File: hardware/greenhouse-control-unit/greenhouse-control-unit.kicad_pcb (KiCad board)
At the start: 4 copper layers, 150 x 90 mm, 53 parts, among them J1 Buck_Conn_01x01_Female, J10 Conn_ESP32_DevKitV1_Female, J12 Conn_01x05_Female, J13 Beep_Jumper, J15 Conn_01x05_Female, J16 Conn_01x05_Female, J2 Buck_Conn_01x01_Female, J3 Buck_Conn_01x01_Female, J4 Buck_Conn_01x01_Female, J5 Molex_KK-396_01x02, J6 Molex_KK-396_01x02, J7 Molex_KK-396_01x12, J8 Molex_KK-254_01x12, J9 Conn_01x09, Q1 BC547, Q2 BC547, Q3 BC547, Q4 BC547, Q5 2N3906, Q7 BC337, Q8 BC337, U1 PCF8574

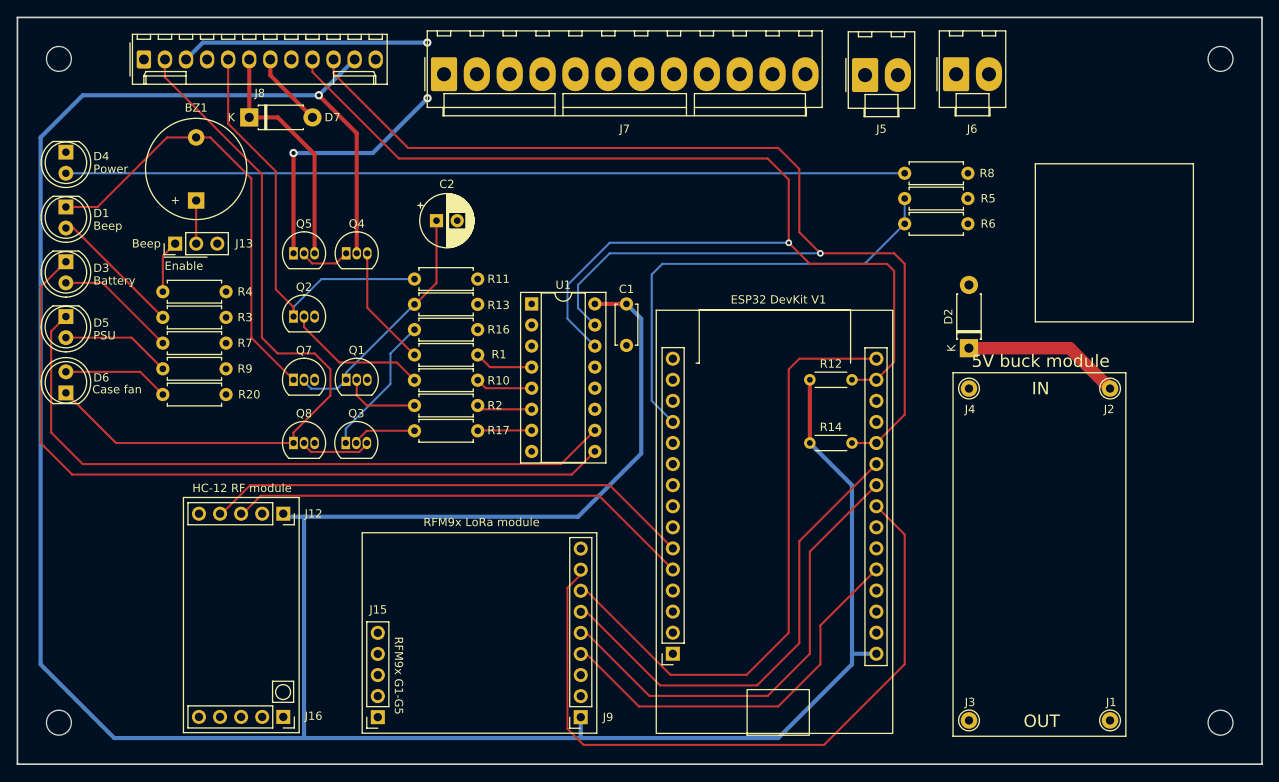
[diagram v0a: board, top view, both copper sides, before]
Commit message: Tidied up PCB
Repositioned power connectors
Resized power layer areas
Tidied up nets
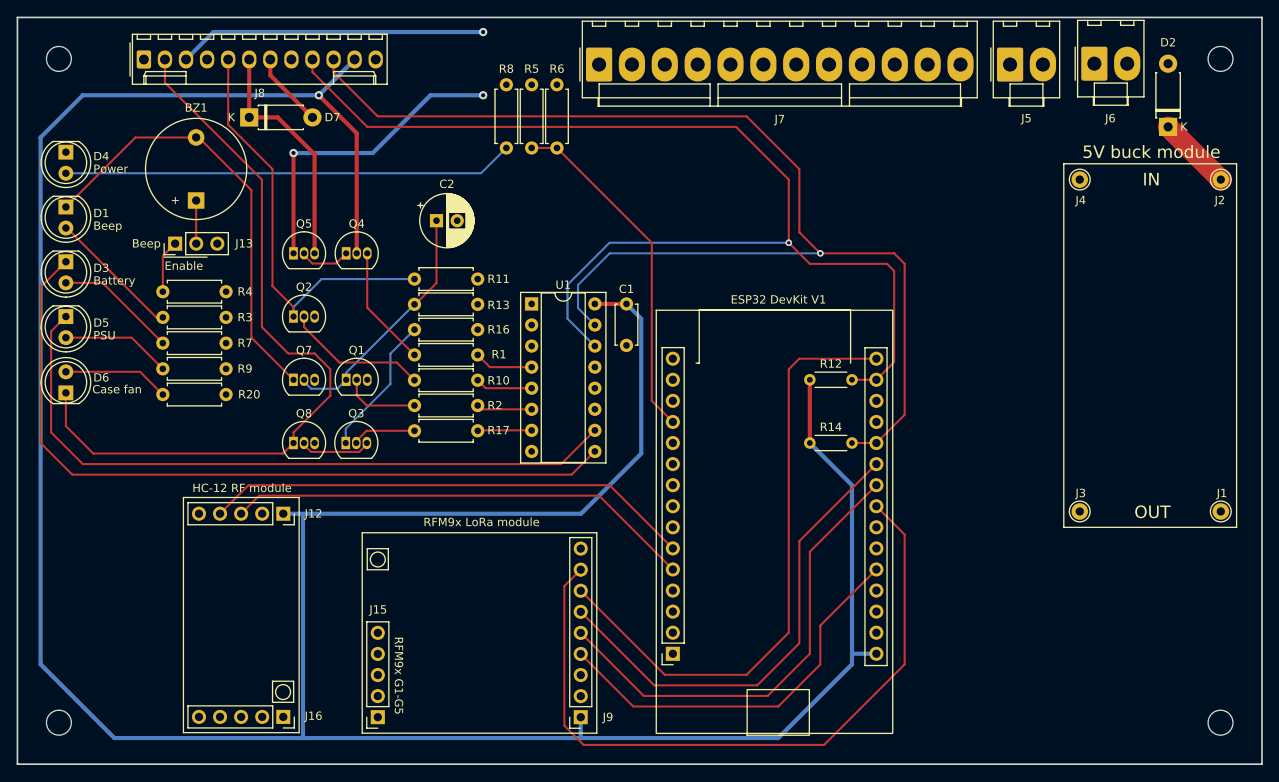
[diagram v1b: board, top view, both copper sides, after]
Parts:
- moved R8 56.6 mm to (131.1, 52.6), turned to -90 degrees
- moved R5 54.3 mm to (134.1, 52.6), turned to -90 degrees
- moved R6 42.9 mm to (137.2, 60.2), turned to 90 degrees
- moved D2 35.9 mm to (210.8, 57.7)
- moved J1 28.5 mm to (217.2, 104.0)
- moved J2 28.5 mm to (217.2, 64.0)
- moved J3 28.5 mm to (200.2, 104.0)
- moved J4 28.5 mm to (200.2, 64.0)
- moved J7 18.7 mm to (142.2, 50.1)
- moved J5 17.5 mm to (191.8, 50.1)
- moved J6 16.7 mm to (201.9, 50.0)
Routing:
- net Net-(D4-Pad2): track 101.1 -> 54.3 mm
- net +12V: track 60.9 -> 75.0 mm
- net /VSense: track 54.9 -> 41.9 mm
- net /Buck+12V: track 19.0 -> 8.98 mm
- net /CaseFan_Sink: track 88.9 -> 91.5 mm
- net Net-(BZ1-Pad2): track 54.2 -> 53.4 mm
- net +3V3: track 368.3 -> 368.9 mm
- net /SCLK: track 55.9 -> 56.5 mm
- net /RFM95_IRQ: track 47.2 -> 47.8 mm
- net /MOSI: track 73.6 -> 74.2 mm
- net /MISO: track 56.9 -> 57.6 mm

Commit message: Swapped 5V and 3V3 power planes
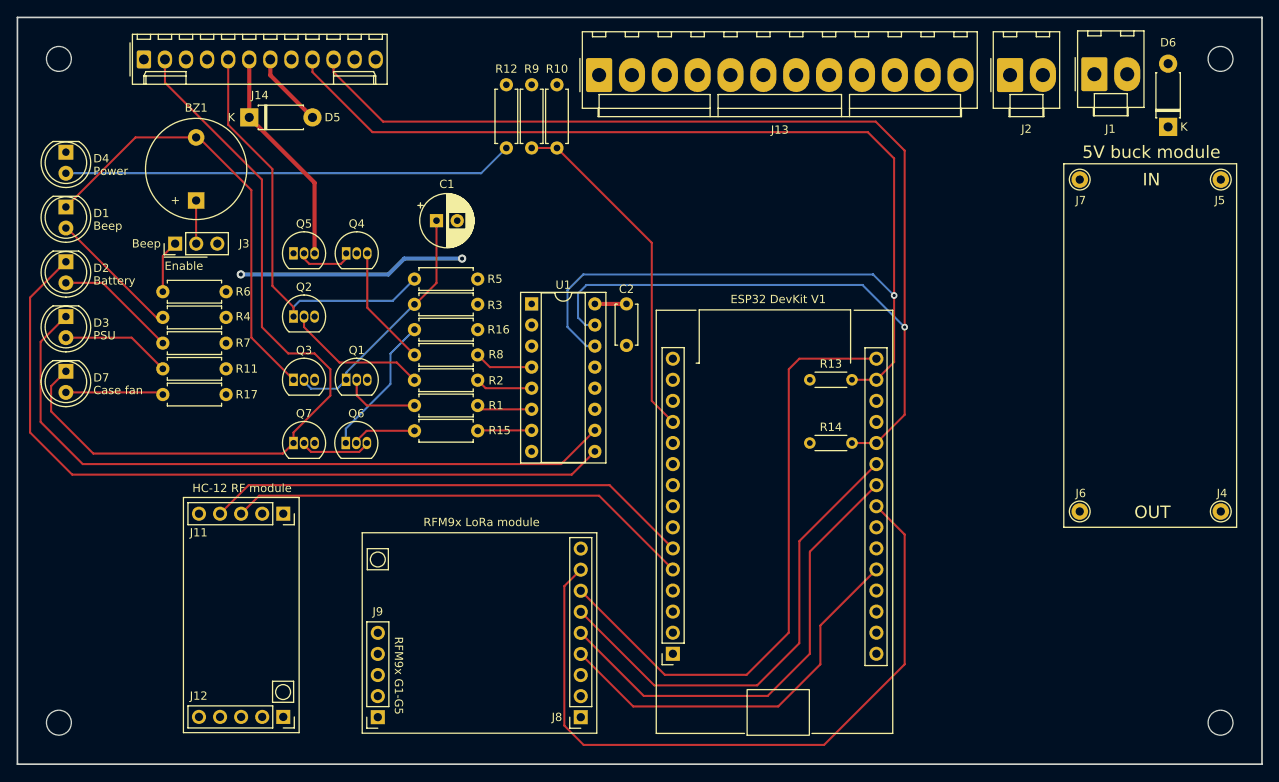
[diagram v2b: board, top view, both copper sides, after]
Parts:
- BZ1: value 10mA beep -> Buzzer
- C1: renamed from C2; value 100uF -> C_Polarized_Small
- C2: renamed from C1; value 10nF -> C_Small
- D5: renamed from D7; value FR107 -> D
- J1: renamed from J6; value Molex_KK-396_01x02 -> Conn_01x02_Male
- J13: renamed from J7; value Molex_KK-396_01x12 -> Conn_01x12_Male
- J14: renamed from J8; value Molex_KK-254_01x12 -> Conn_01x12_Male
- J2: renamed from J5; value Molex_KK-396_01x02 -> Conn_01x02_Male
- J3: renamed from J13; value Beep_Jumper -> Conn_01x03_Female
- J4: renamed from J1; value Buck_Conn_01x01_Female -> Conn_01x01_Male
- J5: renamed from J2; value Buck_Conn_01x01_Female -> Conn_01x01_Male
- J6: renamed from J3; value Buck_Conn_01x01_Female -> Conn_01x01_Male
- J7: renamed from J4; value Buck_Conn_01x01_Female -> Conn_01x01_Male
- J8: renamed from J9; value Conn_01x09 -> Conn_01x09_Female
- R1: renamed from R2; value 33k -> R_US
- R10: renamed from R6; value 220k -> R_US
- R11: renamed from R9; value 2k -> R_US
- R12: renamed from R8; value 10k -> R_US
- R13: renamed from R12; value 10k -> R_US
- R14: value 10k -> R_US
- R15: renamed from R17; value 33k -> R_US
- R16: value 1k -> R_US
- R17: renamed from R20; value 2k -> R_US
- R2: renamed from R10; value 33k -> R_US
- R3: renamed from R13; value 1k -> R_US
- R4: renamed from R3; value 2k -> R_US
- R5: renamed from R11; value 1k -> R_US
- R6: renamed from R4; value 100R -> R_US
- R7: value 2k -> R_US
- R8: renamed from R1; value 1k -> R_US
- R9: renamed from R5; value 1M -> R_US
- moved D7 2.60 mm to (78.0, 87.1), turned to -90 degrees
- moved J1 1.27 mm to (201.9, 51.3)
- moved J13 1.27 mm to (142.2, 51.4)
- moved J2 1.27 mm to (191.8, 51.4)
- renumbered D3 to D2, D5 to D3, D2 to D6, D6 to D7, J12 to J11, J16 to J12, J15 to J9, Q7 to Q3, Q3 to Q6, Q8 to Q7
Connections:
- J1 pad 1: /Batt+12V -> +12V
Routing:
- net +3V3: track 368.9 -> 3.81 mm, vias 1 -> 0
- net +5V: track 0.00 -> 260.8 mm, vias 0 -> 2
- net /I2C_SCL: track 140.5 -> 156.3 mm
- net /I2C_SDA: track 146.8 -> 161.1 mm
- net +12V: track 75.0 -> 68.7 mm, vias 3 -> 0
- net /CaseFan_Sink: track 91.5 -> 95.6 mm
- net /BattRelayNC_A: track 28.6 -> 26.6 mm
- net Net-(D7-Pad2): track 12.9 -> 11.8 mm
- net /IO_PsuLed: track 83.5 -> 84.6 mm
- net /IO_BatteryLed: track 92.6 -> 93.7 mm
- net Net-(Q4-Pad1): track 6.00 -> 6.88 mm
- added copper zone on In1.Cu, net +3V3

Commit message: Export fab files
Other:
- board text added: "Greenhouse Control Unit"
- board text added: "Nick Bolton"
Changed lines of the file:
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@@
       (outputformat 1)
       (mirror false)
-      (drillshape 1)
+      (drillshape 0)
       (scaleselection 1)
-      (outputdirectory "")
+      (outputdirectory "fab/")
     )
   )
@@
     (fp_line (start -0.005 3.895) (end -1.91 3.895) (layer "F.Fab") (width 0.1))
     (fp_line (start 5.87 -5.11) (end 5.87 3.895) (layer "F.Fab") (width 0.1))
-    (pad "1" thru_hole roundrect (at 0 0) (size 3.16 4.1) (drill 1.7) (layers *.Cu *.Mask) (roundrect_rratio 0.079114)
+    (pad "1" thru_hole roundrect (at 0 0) (size 3.16 4.1) (drill 1.7) (layers *.Cu *.Mask) (roundrect_rratio 0.07911392405)
       (net 16 "+12V") (pinfunction "Pin_1") (pintype "passive"))
     (pad "2" thru_hole oval (at 3.96 0) (size 3.16 4.1) (drill 1.7) (layers *.Cu *.Mask)
@@
     (fp_line (start 29.21 -2.92) (end -1.27 -2.92) (layer "F.Fab") (width 0.1))
     (fp_line (start -1.27 2.88) (end 29.21 2.88) (layer "F.Fab") (width 0.1))
-    (pad "1" thru_hole roundrect (at 0 0) (size 1.74 2.19) (drill 1.19) (layers *.Cu *.Mask) (roundrect_rratio 0.143678)
+    (pad "1" thru_hole roundrect (at 0 0) (size 1.74 2.19) (drill 1.19) (layers *.Cu *.Mask) (roundrect_rratio 0.1436781609)
       (net 3 "+5V") (pinfunction "Pin_1") (pintype "passive"))
     (pad "2" thru_hole oval (at 2.54 0) (size 1.74 2.19) (drill 1.19) (layers *.Cu *.Mask)
@@
     (fp_line (start 5.87 3.895) (end 3.965 3.895) (layer "F.Fab") (width 0.1))
     (fp_line (start -0.005 3.895) (end -1.91 3.895) (layer "F.Fab") (width 0.1))
-    (pad "1" thru_hole roundrect (at 0 0) (size 3.16 4.1) (drill 1.7) (layers *.Cu *.Mask) (roundrect_rratio 0.079114)
+    (pad "1" thru_hole roundrect (at 0 0) (size 3.16 4.1) (drill 1.7) (layers *.Cu *.Mask) (roundrect_rratio 0.07911392405)
       (net 16 "+12V") (pinfunction "Pin_1") (pintype "passive"))
     (pad "2" thru_hole oval (at 3.96 0) (size 3.16 4.1) (drill 1.7) (layers *.Cu *.Mask)
@@
     (fp_line (start -1.202893 0) (end -1.91 0.5) (layer "F.Fab") (width 0.1))
     (fp_line (start 43.565 4.9) (end -0.005 4.9) (layer "F.Fab") (width 0.1))
-    (pad "1" thru_hole roundrect (at 0 0) (size 3.16 4.1) (drill 1.7) (layers *.Cu *.Mask) (roundrect_rratio 0.079114)
+    (pad "1" thru_hole roundrect (at 0 0) (size 3.16 4.1) (drill 1.7) (layers *.Cu *.Mask) (roundrect_rratio 0.07911392405)
       (net 16 "+12V") (pinfunction "Pin_1") (pintype "passive"))
     (pad "2" thru_hole oval (at 3.96 0) (size 3.16 4.1) (drill 1.7) (layers *.Cu *.Mask)
@@
     (effects (font (size 1.5 1.5) (thickness 0.25)))
   )
+  (gr_text "Nick Bolton" (at 181.61 130.048) (layer "F.SilkS")
+    (effects (font (size 1.5 1.5) (thickness 0.3)) (justify left))
+  )
   (gr_text "5V buck module" (at 208.806 60.706) (layer "F.SilkS")
     (effects (font (size 1.5 1.5) (thickness 0.25)))
   )
+  (gr_text "Greenhouse Control Unit" (at 181.61 127.508) (layer "F.SilkS")
+    (effects (font (size 1.5 1.5) (thickness 0.3)) (justify left))
+  )
   (gr_text "IN" (at 208.806 64.008) (layer "F.SilkS")

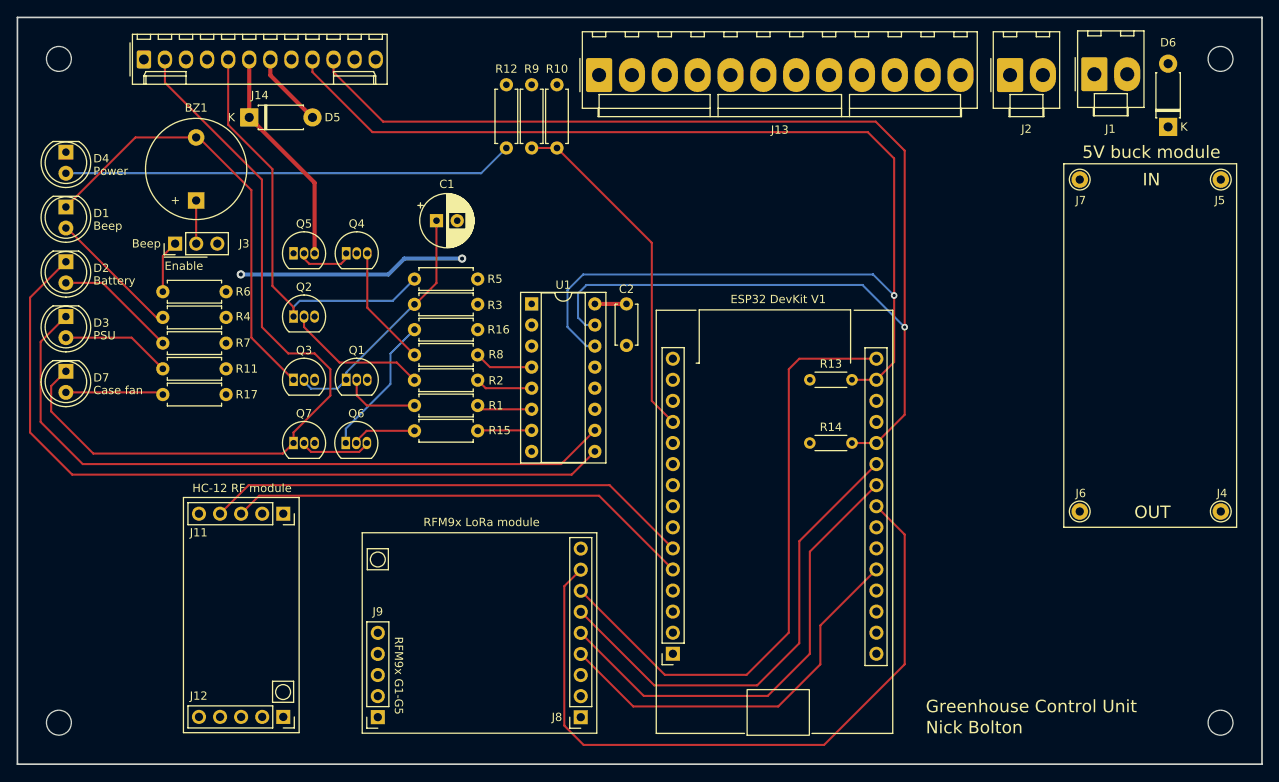
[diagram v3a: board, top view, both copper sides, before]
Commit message: Applied values to parts
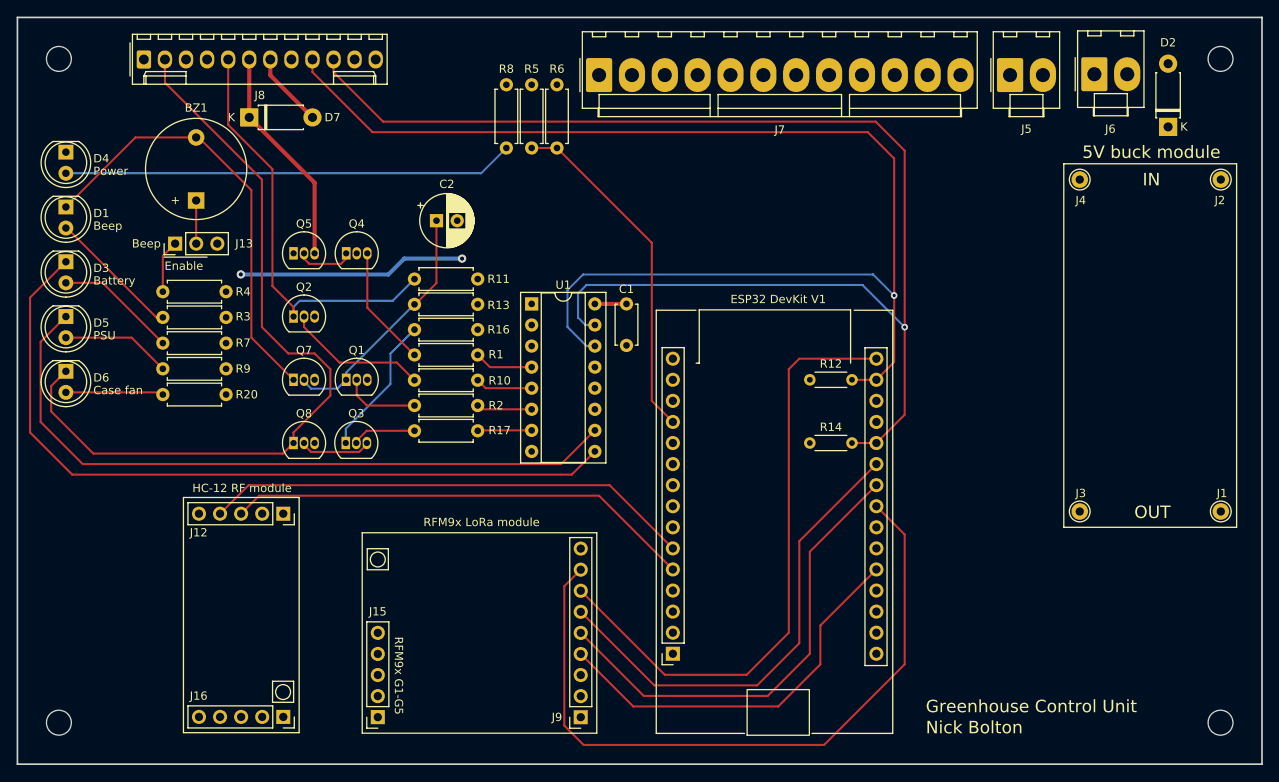
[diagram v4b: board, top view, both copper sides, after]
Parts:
- BZ1: value Buzzer -> 10mA beep
- C1: renamed from C2; value C_Small -> 10nF
- C2: renamed from C1; value C_Polarized_Small -> 100uF
- D7: renamed from D5; value D -> FR107
- J13: renamed from J3; value Conn_01x03_Female -> Beep_Jumper
- J5: renamed from J2; value Conn_01x02_Male -> Molex_KK-396_01x02
- J6: renamed from J1; value Conn_01x02_Male -> Molex_KK-396_01x02
- J7: renamed from J13; value Conn_01x12_Male -> Molex_KK-396_01x12
- J8: renamed from J14; value Conn_01x12_Male -> Molex_KK-254_01x12
- J9: renamed from J8; value Conn_01x09_Female -> Conn_01x09
- R1: renamed from R8; value R_US -> 1k
- R10: renamed from R2; value R_US -> 33k
- R11: renamed from R5; value R_US -> 1k
- R12: renamed from R13; value R_US -> 10k
- R13: renamed from R3; value R_US -> 1k
- R14: value R_US -> 10k
- R16: value R_US -> 1k
- R17: renamed from R15; value R_US -> 33k
- R2: renamed from R1; value R_US -> 33k
- R20: renamed from R17; value R_US -> 2k
- R3: renamed from R4; value R_US -> 2k
- R4: renamed from R6; value R_US -> 100R
- R5: renamed from R9; value R_US -> 1M
- R6: renamed from R10; value R_US -> 220k
- R7: value R_US -> 2k
- R8: renamed from R12; value R_US -> 10k
- R9: renamed from R11; value R_US -> 2k
- renumbered D6 to D2, D2 to D3, D3 to D5, D7 to D6, J4 to J1, J11 to J12, J9 to J15, J12 to J16, J5 to J2, J6 to J3, J7 to J4, Q6 to Q3, Q3 to Q7, Q7 to Q8
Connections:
- J6 pad 1: +12V -> /Batt+12V

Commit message: Fixed annotation references
Somehow became different to PCB run
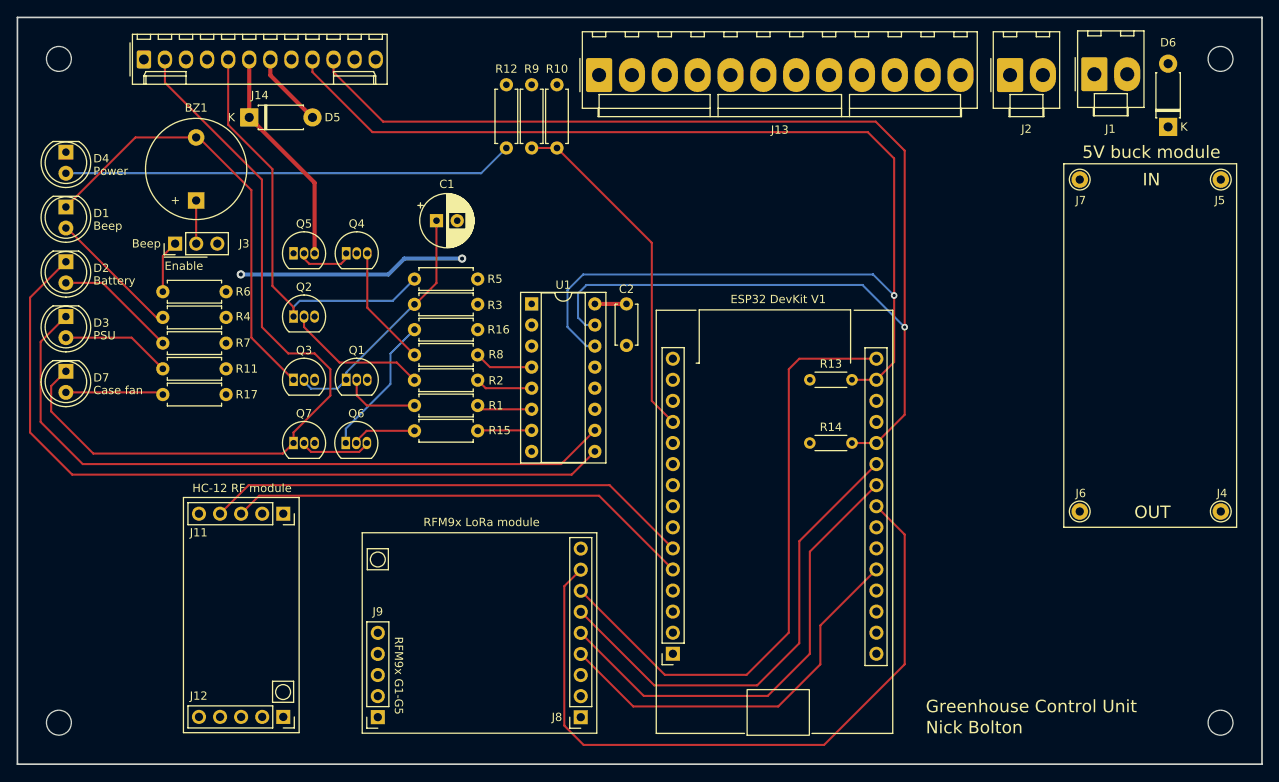
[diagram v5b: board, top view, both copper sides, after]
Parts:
- renumbered C2 to C1, C1 to C2, D3 to D2, D5 to D3, D7 to D5, D2 to D6, D6 to D7, J6 to J1, J12 to J11, J16 to J12, J7 to J13, J8 to J14, J5 to J2, J13 to J3, J1 to J4, J2 to J5, J3 to J6, J4 to J7, J9 to J8, J15 to J9, Q7 to Q3, Q3 to Q6, Q8 to Q7, R2 to R1, R6 to R10, R9 to R11, R8 to R12, R12 to R13, R17 to R15, R20 to R17, R10 to R2, R13 to R3, R3 to R4, R11 to R5, R4 to R6, R1 to R8, R5 to R9
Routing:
- net /IO_Beep: track 6.05 -> 6.69 mm

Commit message: Fixed beep pull-up cap value
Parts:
- C1: value 100uF -> 220uF
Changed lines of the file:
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@@
       (effects (font (size 1 1) (thickness 0.15)))
     )
-    (fp_text value "100uF" (at 1.25 4.4) (layer "F.Fab")
+    (fp_text value "220uF" (at 1.25 4.4) (layer "F.Fab")
       (effects (font (size 1 1) (thickness 0.15)))
     )
